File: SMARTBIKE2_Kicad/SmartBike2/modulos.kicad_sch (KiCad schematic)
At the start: 9 parts, among them J3 Conn_01x05, J4 Conn_01x06, J5 Conn_01x08, J6 Conn_01x04, Q10 SI2302, Q9 FDN340P

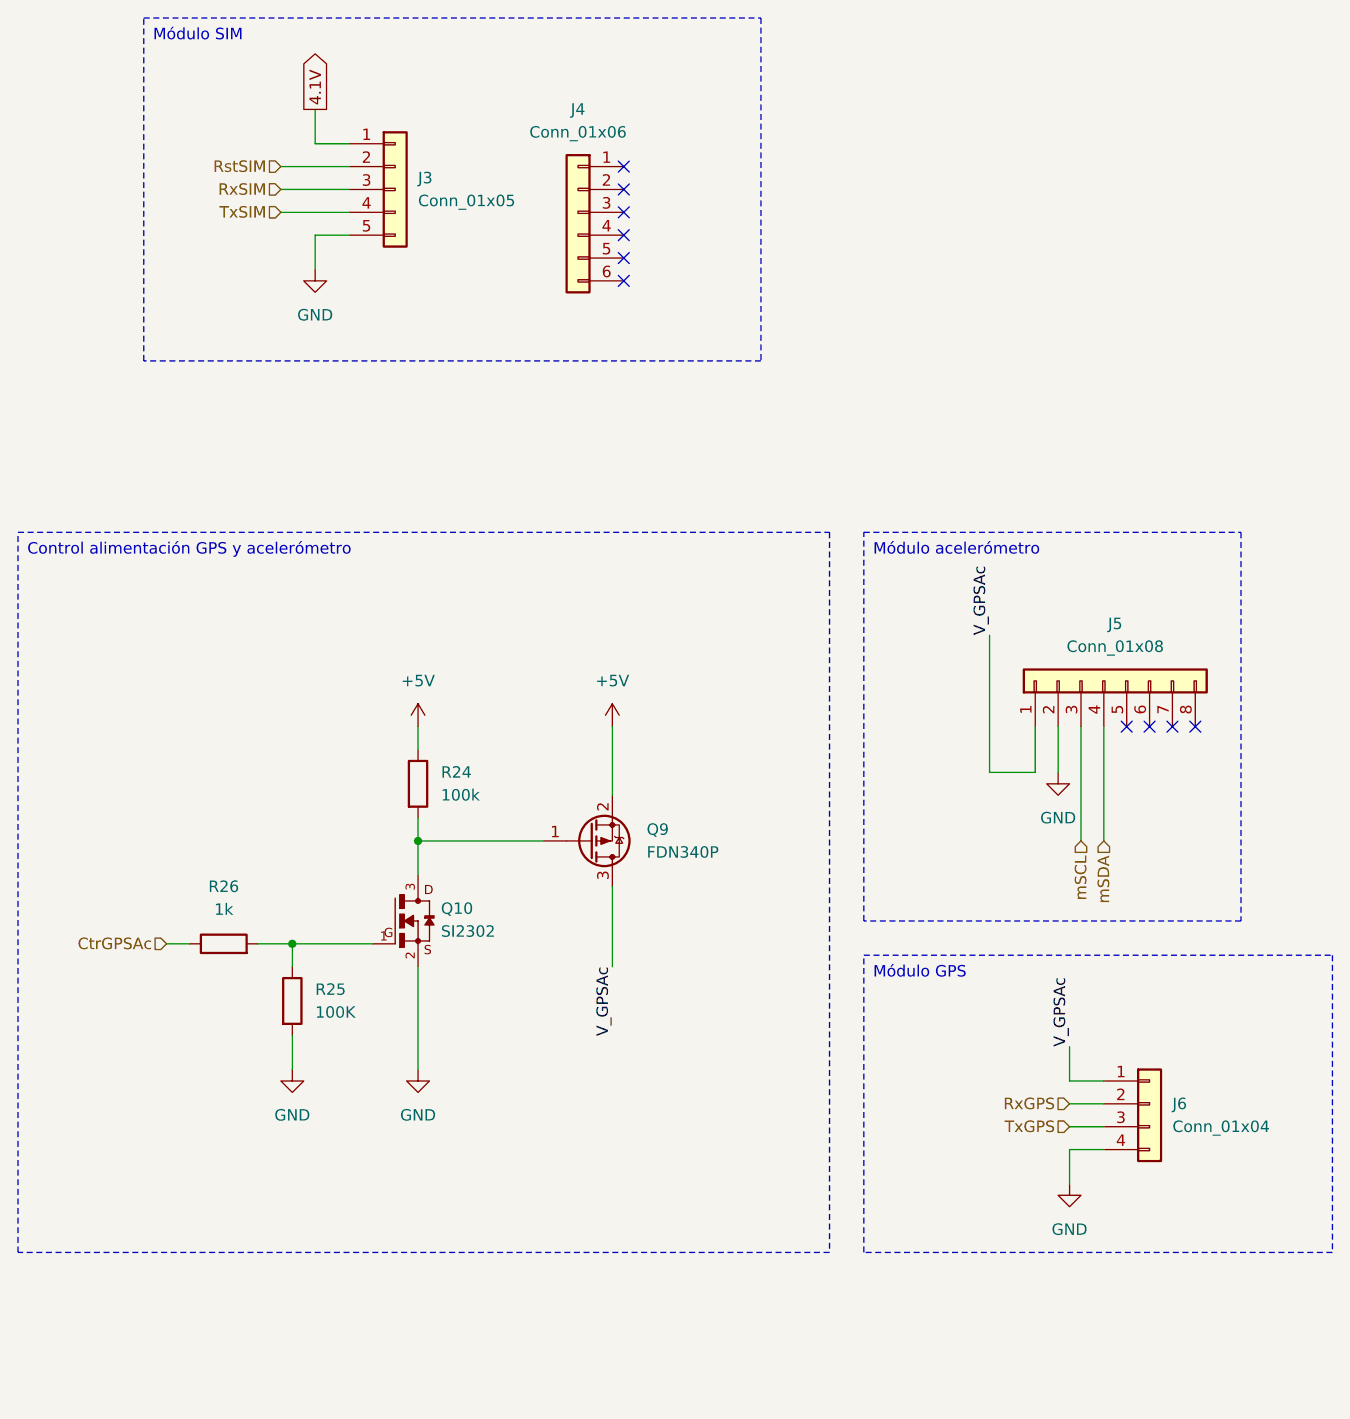
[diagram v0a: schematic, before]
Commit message: Beta 100% esquemáticos
+ Acondicionamiento ESP32

~ Huellas
~ PCB
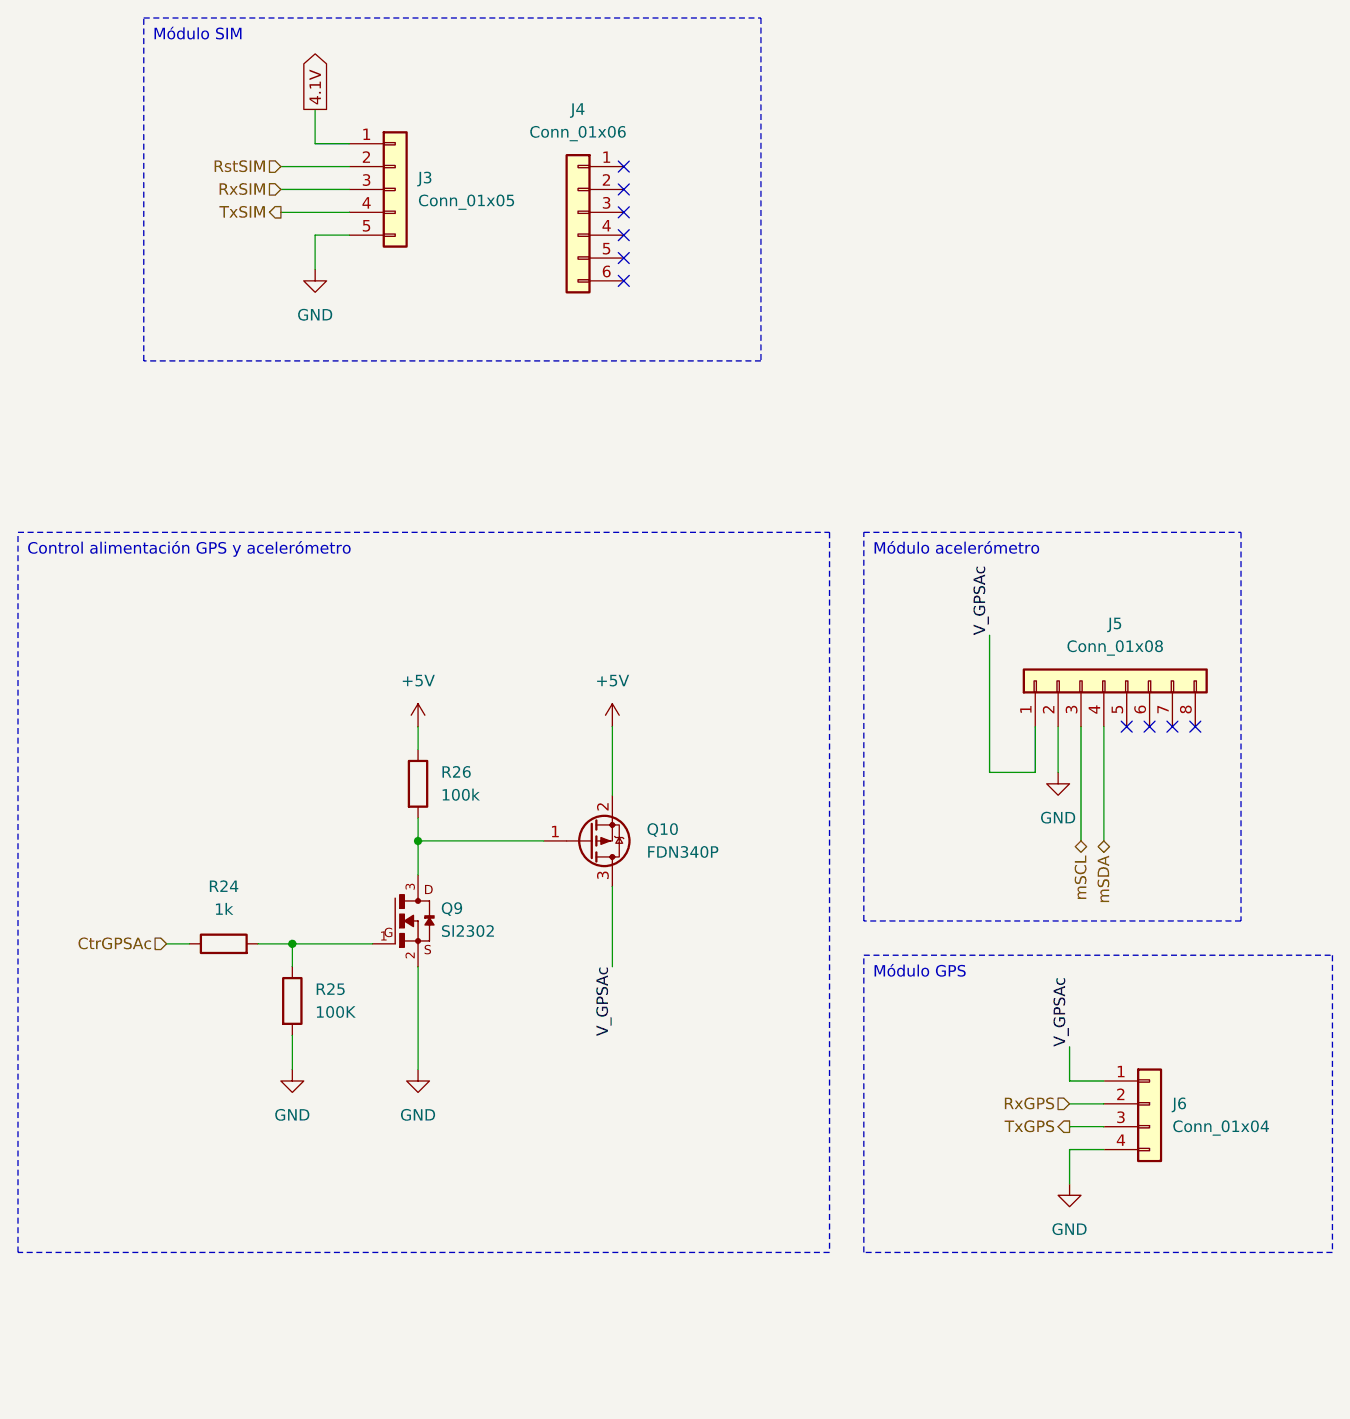
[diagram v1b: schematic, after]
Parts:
- renumbered Q9 to Q10, Q10 to Q9, R26 to R24, R24 to R26

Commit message: cambio alimentacion GPS
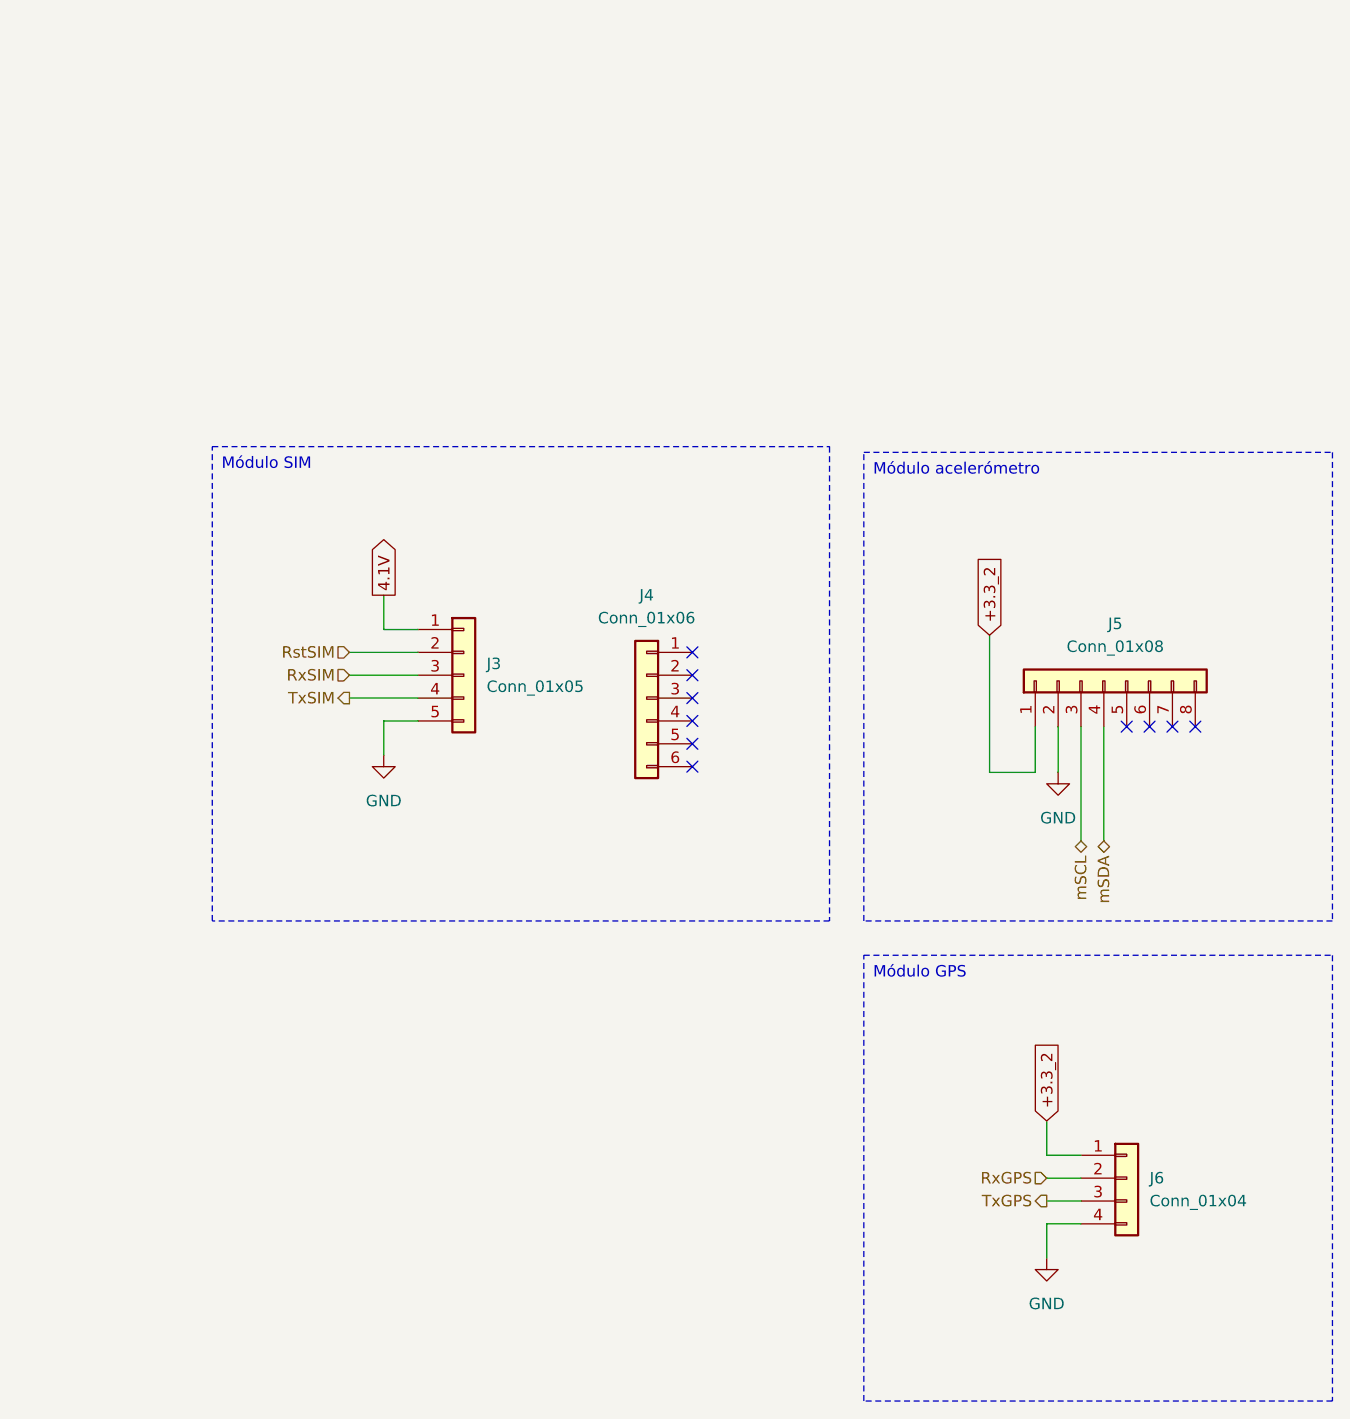
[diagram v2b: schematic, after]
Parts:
- removed Q10: FDN340P, Package_TO_SOT_SMD:SOT-23, symbol Transistor_FET:FDN340P
- removed Q9: SI2302, SI2302:SOT23, symbol SI2302:SI2302
- removed R24: 1k, symbol Device:R
- removed R25: 100K, symbol Device:R
- removed R26: 100k, symbol Device:R
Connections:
- net V_GPSAc renamed +3.3_2
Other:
- moved on the sheet: J3, J4, J6

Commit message: mas huellas
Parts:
- J3: footprint (none) -> Connector_PinSocket_2.54mm:PinSocket_1x05_P2.54mm_Vertical
- J4: footprint (none) -> Connector_PinSocket_2.54mm:PinSocket_1x06_P2.54mm_Vertical
- J5: footprint (none) -> Connector_PinSocket_2.54mm:PinSocket_1x08_P2.54mm_Vertical
- J6: footprint (none) -> Connector_PinSocket_2.54mm:PinSocket_1x04_P2.54mm_Vertical
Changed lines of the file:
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@@
       (effects (font (size 1.27 1.27)))
     )
-    (property "Footprint" "" (at 143.51 104.14 0)
+    (property "Footprint" "Connector_PinSocket_2.54mm:PinSocket_1x08_P2.54mm_Vertical" (at 143.51 104.14 0)
       (effects (font (size 1.27 1.27)) hide)
     )
@@
       (effects (font (size 1.27 1.27)))
     )
-    (property "Footprint" "" (at 92.71 106.045 0)
+    (property "Footprint" "Connector_PinSocket_2.54mm:PinSocket_1x06_P2.54mm_Vertical" (at 92.71 106.045 0)
       (effects (font (size 1.27 1.27)) hide)
     )
@@
       (effects (font (size 1.27 1.27)) (justify left))
     )
-    (property "Footprint" "" (at 72.39 103.505 0)
+    (property "Footprint" "Connector_PinSocket_2.54mm:PinSocket_1x05_P2.54mm_Vertical" (at 72.39 103.505 0)
       (effects (font (size 1.27 1.27)) hide)
     )
@@
       (effects (font (size 1.27 1.27)) (justify left))
     )
-    (property "Footprint" "" (at 146.05 159.385 0)
+    (property "Footprint" "Connector_PinSocket_2.54mm:PinSocket_1x04_P2.54mm_Vertical" (at 146.05 159.385 0)
       (effects (font (size 1.27 1.27)) hide)
     )
